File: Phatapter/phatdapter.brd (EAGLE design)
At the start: 65 x 78.4 mm, 75 parts, among them J1 RASPBERRYPI-40-PIN-GPIO_SMD_M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, J2 RASPBERRYPI-40-PIN-GPIO_RIGHT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, J3 QWIIC_RIGHT_ANGLE, J5 QWIIC_RIGHT_ANGLE

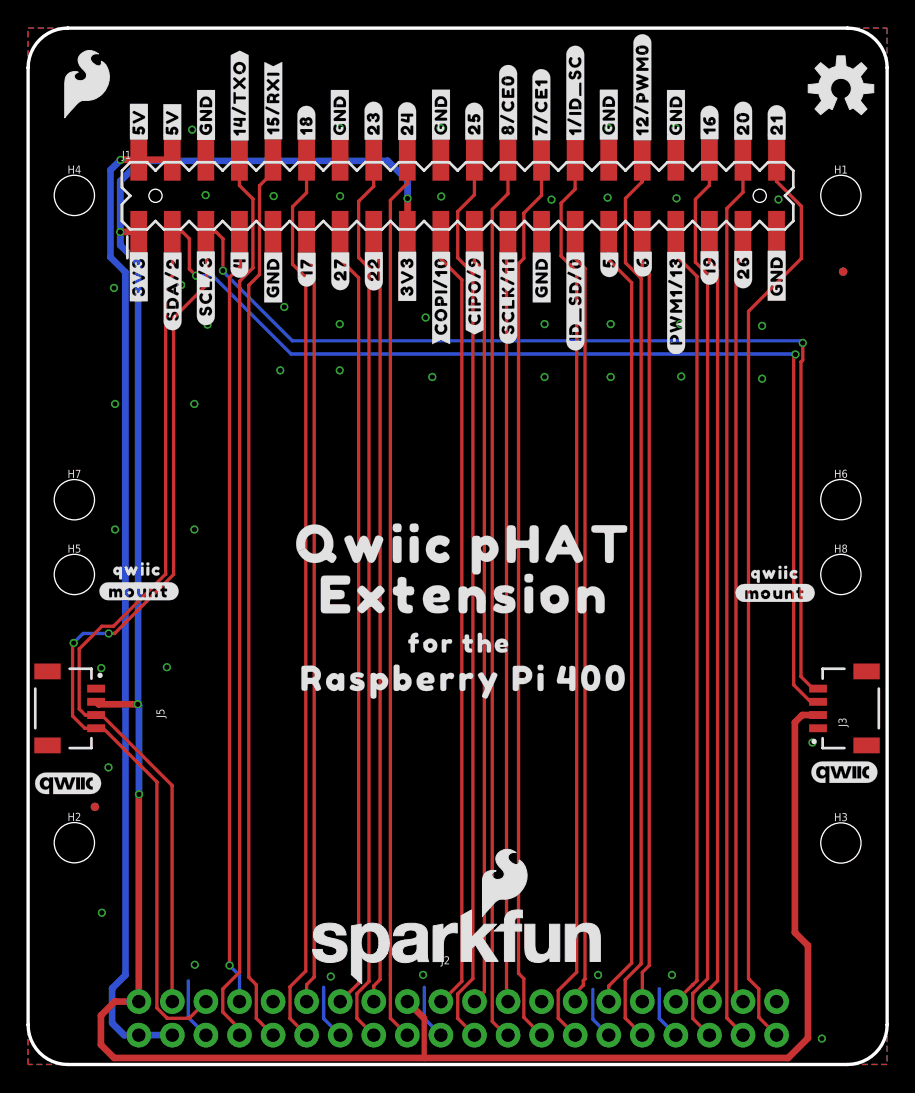
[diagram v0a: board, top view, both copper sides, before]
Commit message: Moves standoffs for Qwiic mount because it would have interfered with micro Raspberry hats
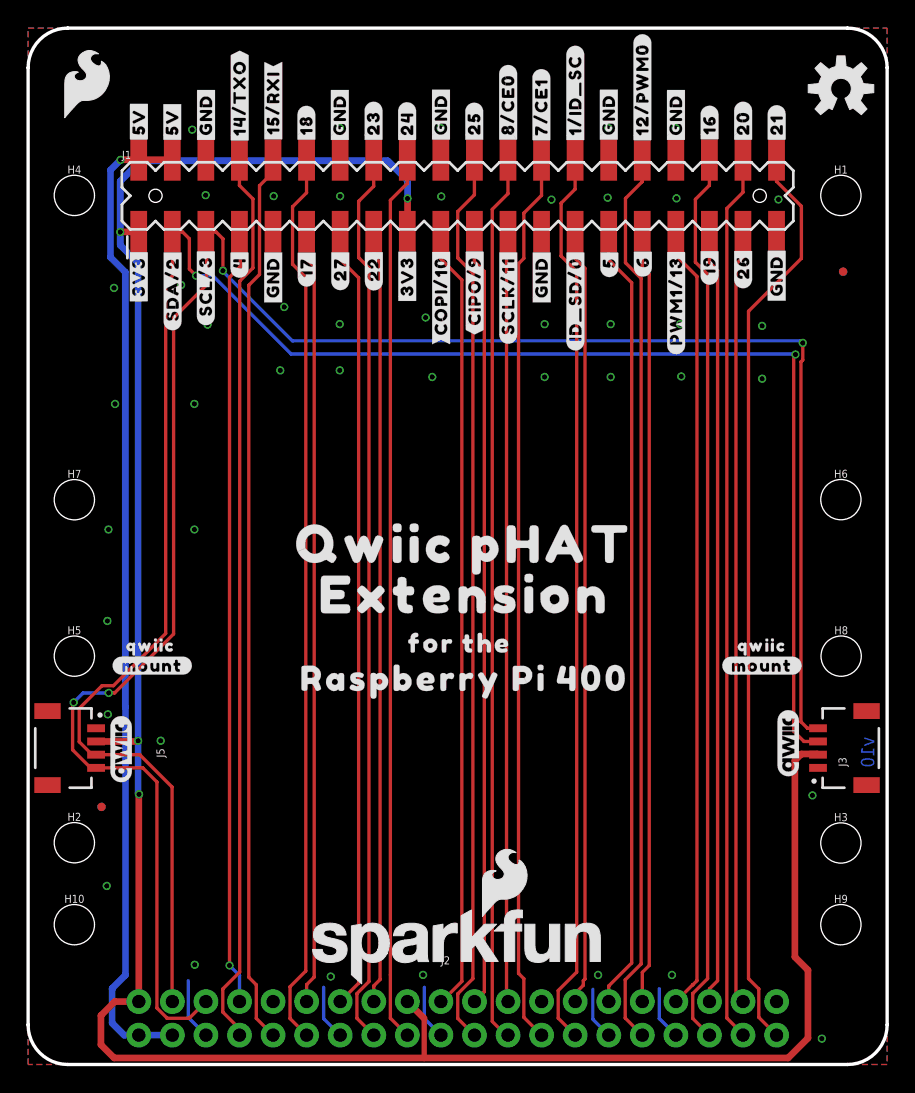
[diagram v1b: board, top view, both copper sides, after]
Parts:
- added H10, H9: STAND-OFFTIGHT, SparkFun-Hardware:STAND-OFF-TIGHT
- moved H8 6.18 mm to (61.5, 30.9)
- moved H5 6.18 mm to (3.49, 30.9)
- moved U$84 5.84 mm to (9.26, 31.7)
- moved U$82 5.72 mm to (9.38, 30.2)
- moved U$85 5.59 mm to (55.5, 31.7)
- moved U$83 5.59 mm to (55.5, 30.2)
- moved LOGO1 4.76 mm to (7.01, 23.8), turned to 90 degrees
- moved LOGO4 4.75 mm to (57.5, 24.3), turned to 90 degrees
- moved J3 3.00 mm to (59.8, 23.9)
- moved J5 3.00 mm to (5.13, 23.9)
- moved FD1 0.50 mm to (5.54, 19.5)
- moved FD4 0.50 mm to (5.54, 19.5)
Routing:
- net 3/SCL: track 149.4 -> 154.2 mm
- net 2/SDA: track 145.1 -> 149.8 mm
- net 3.3V: track 185.4 -> 182.4 mm
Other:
- board text added: "v10"
